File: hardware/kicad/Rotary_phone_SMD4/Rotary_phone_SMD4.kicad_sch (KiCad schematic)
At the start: 64 parts, among them J1 Barrel_Jack_PTH_Slot, J3 PINHD_1x2_Male, J4 PINHD_1x2_Male, J5 PINHD_2x4_Male, J7 PINHD_1x3_Male, J8 RJ12, J9 RJ12, U1 ESP32-C6-DevKitC-1, U2 ES8388, U3 AG1171, U4 AG1171

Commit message: Add SMD4 board support, WiFi setup UX (SSID scan, reset buttons, DHCP hostname)
SMD4 bring-up:
- New board_pins_smd4.h pin map (verified against schematic), Kconfig
  choice, and CMake/preprocessor fixes so es8388/wm8731 build correctly
  for the new board type alongside SMD2/THT.
- Bringup script comment fixes (test_audio.py) for boards past the
  SMD2-only ADC mux bodge.

WiFi/setup UX:
- Live SSID scan (wifi_scan()) with a dropdown picker (+ manual-entry
  fallback) on both the captive setup page and Settings -> General,
  replacing free-text SSID entry.
- Setup AP renamed RotaryPhone-XXXX -> AnalogRedial-XXXX.
- DHCP hostname now set from the board name (was the generic
  "espressif" default) so a router's client list shows something
  identifiable.
- Post-setup confirmation page gives the actual .local address to try
  and recommends the router's client list as a same-weight fallback,
  not a last resort.
- New Settings -> Hardware "Reset" card: re-provision WiFi only (keeps
  all other settings) and a full factory reset (erases all NVS,
  leaves recordings/uploads untouched).

Also: dual idle-power presets, Storage/Diagnostics load-time fixes,
Dial Codes tab redesign, dark-mode link contrast fix, simplified
favicon -- carried over from the same working session.

Co-Authored-By: Claude Sonnet 5 <noreply@anthropic.com>
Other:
- note added: "Fixes needed for SMD4: capacitor silkscreen needs to show capacitance value larger holes for esp32 silkscreen note to add jumpbers for 2nd AG1171"
- note removed: "Fixes: 470 uF capacitors are 8mm/3.5 pitch add reset jumper Fix cross-wired usb D+/D- Connect redundant usb-c wires so cables work in both directions In/out audio lines were swapped! Change Line0/1 in/out to mic for better readability Move Ch2 mic from Lin2 to Rin1 to fix error Todo: cleaner routing for USB D+/D- ? Test use of single P6KE82"
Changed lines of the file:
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@@
 		)
 	)
-	(text "Fixes:\n470 uF capacitors are 8mm/3.5 pitch\nadd reset jumper\nFix cross-wired usb D+/D-\nConnect redundant usb-c wires so cables work in both directions\nIn/out audio lines were swapped!\nChange Line0/1 in/out to mic for better readability\nMove Ch2 mic from Lin2 to Rin1 to fix error\n\nTodo: \ncleaner routing for USB D+/D- ?\nTest use of single P6KE82"
+	(text "Fixes needed for SMD4:\ncapacitor silkscreen needs to show capacitance value\nlarger holes for esp32\nsilkscreen note to add jumpbers for 2nd AG1171\n"
 		(exclude_from_sim no)
 		(at 243.84 41.402 0)

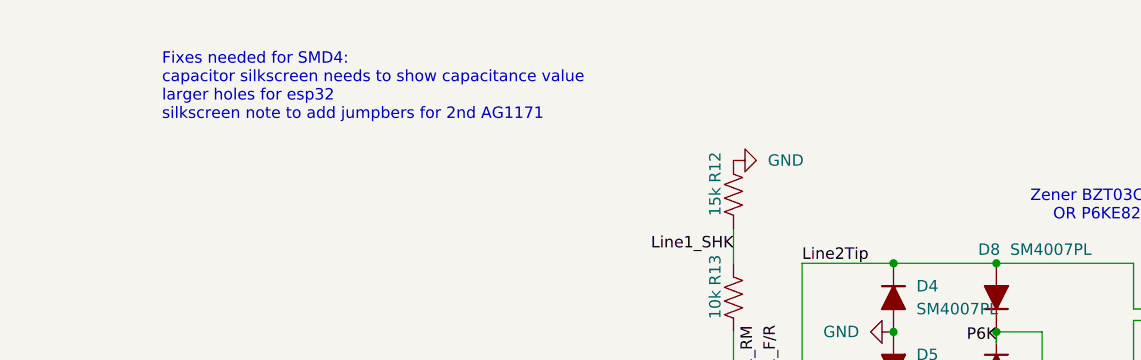
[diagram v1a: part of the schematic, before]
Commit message: Add live memory-map card; fix board type display; simplify hw-config card
- New Settings -> Hardware "Memory map" card: RAM used/free, and every
  flash partition actually in the live partition table (via
  esp_partition_find(), not a copy of partitions.csv baked into the
  UI) with real usage where available (storage/bundled file sizes, NVS
  entry stats) plus a plain answer to "would an 8MB flash chip fit
  this layout" using today's real numbers.
- Fixed two real bugs found while building it: esp_partition_next()
  releases its iterator internally once it reaches the end of the
  list, so an extra esp_partition_iterator_release() call after the
  loop (and, worse, reusing the same iterator across two separate
  loops) double-freed it -- a real, reproducible TLSF heap-corruption
  crash on every load of this card, not a hypothetical. Also fixed two
  fmt_bytes() calls sharing one output buffer as sibling arguments to
  the same snprintf(), which under C's unspecified evaluation order
  could show the wrong figure for RAM total.
- board_hardware_str() always reported "(SMD2)" regardless of which
  PCB the firmware was actually built for -- board_current_type()
  deliberately collapses SMD2/SMD4 into one BOARD_TYPE_SMD (they share
  the line2/microSD GPIO tradeoff), so it was never the right thing to
  read this from. New board_pcb_variant_name() reports the precise
  compile-time PCB name instead, kept separate on purpose.
- Line 2/microSD config card: moved its long explanation from the top
  to the bottom (matching every other settings card's layout) and
  trimmed it to plain language -- no GPIO pin numbers, just "jumpers +
  2nd AG1171" vs "no jumpers, microSD works". Same simplification on
  the first-boot banner's copy of this field.

Co-Authored-By: Claude Sonnet 5 <noreply@anthropic.com>
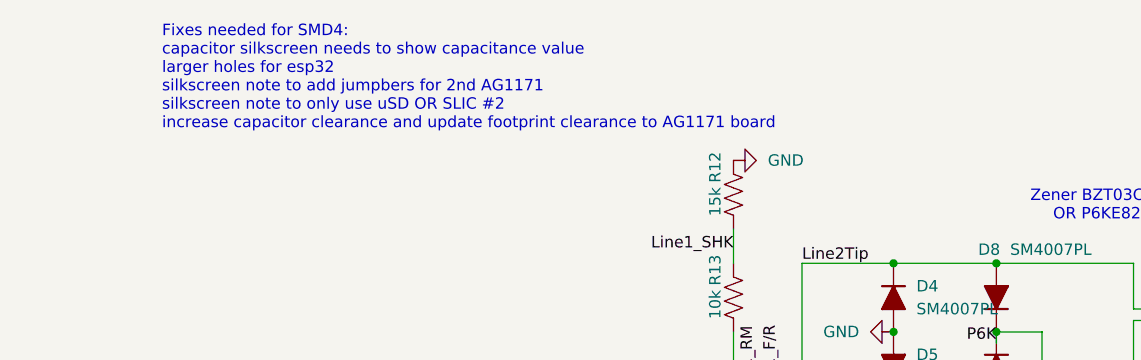
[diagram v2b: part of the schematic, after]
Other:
- note added: "Fixes needed for SMD4: capacitor silkscreen needs to show capacitance value larger holes for esp32 silkscreen note to add jumpbers for 2nd AG1171 silkscreen note to only use uSD OR SLIC #2 increase capacitor clearance and update footprint clearance to AG1171 board"
- note removed: "Fixes needed for SMD4: capacitor silkscreen needs to show capacitance value larger holes for esp32 silkscreen note to add jumpbers for 2nd AG1171"
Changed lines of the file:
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@@
 		)
 	)
-	(text "Fixes needed for SMD4:\ncapacitor silkscreen needs to show capacitance value\nlarger holes for esp32\nsilkscreen note to add jumpbers for 2nd AG1171\n"
+	(text "Fixes needed for SMD4:\ncapacitor silkscreen needs to show capacitance value\nlarger holes for esp32\nsilkscreen note to add jumpbers for 2nd AG1171\nsilkscreen note to only use uSD OR SLIC #2\nincrease capacitor clearance and update footprint clearance to AG1171 board\n\n"
 		(exclude_from_sim no)
 		(at 243.84 41.402 0)

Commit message: kicad: consolidate custom footprints/3D/symbols into libraries/
Move all per-project Scott.pretty, JLCImport.pretty, .3dshapes, and
.kicad_sym files into a single shared kicad/libraries/ directory.
Rename "Scott" library to "Custom" throughout. Update fp-lib-table,
sym-lib-table, .kicad_pcb, and .kicad_sch files in all 6 board
projects to resolve Custom: and JLCImport: via ${KIPRJMOD}/../libraries/.

Also fixes broken 3D model paths (hardcoded /Users/... and
_restore_backup_ references in SMD3/SMD4/AR5 PCBs).

Generated with [Devin](https://devin.ai)

Co-Authored-By: Devin <158243242+devin-ai-integration[bot]@users.noreply.github.com>
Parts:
- J8, J9: footprint Scott:RJ12_Amphenol_87180_Horizontal -> Custom:RJ12_Amphenol_87180_Horizontal
- U3, U4: footprint Scott:AG1171_SIL -> Custom:AG1171_SIL; symbol Scott_Symbol_Library:AG1171_SIL -> Custom_Symbol_Library:AG1171_SIL
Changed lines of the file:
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@@
 			)
 		)
-		(property "Footprint" "Scott:RJ12_Amphenol_87180_Horizontal"
+		(property "Footprint" "Custom:RJ12_Amphenol_87180_Horizontal"
 			(at 364.49 67.945 90)
 			(hide yes)
@@
 			)
 		)
-		(property "Footprint" "Scott:RJ12_Amphenol_87180_Horizontal"
+		(property "Footprint" "Custom:RJ12_Amphenol_87180_Horizontal"
 			(at 367.03 140.335 90)
 			(hide yes)
@@
 	)
 	(symbol
-		(lib_id "Scott_Symbol_Library:AG1171_SIL")
+		(lib_id "Custom_Symbol_Library:AG1171_SIL")
 		(at 308.61 160.02 180)
 		(unit 1)
@@
 			)
 		)
-		(property "Footprint" "Scott:AG1171_SIL"
+		(property "Footprint" "Custom:AG1171_SIL"
 			(at 308.61 160.02 0)
 			(hide yes)
@@
 	)
 	(symbol
-		(lib_id "Scott_Symbol_Library:AG1171_SIL")
+		(lib_id "Custom_Symbol_Library:AG1171_SIL")
 		(at 307.34 87.63 180)
 		(unit 1)
@@
 			)
 		)
-		(property "Footprint" "Scott:AG1171_SIL"
+		(property "Footprint" "Custom:AG1171_SIL"
 			(at 307.34 87.63 0)
 			(hide yes)

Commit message: Consolidate custom KiCad library; point all boards at it
Every custom symbol and footprint this project used to keep in
hardware/kicad/libraries/ (AG1170/AG1171 SIL, the Amphenol/RJ12
connectors, both ESP32-C6 DevKit footprints, WM8731) is now in one
personal library shared across all KiCad projects on this machine:
~/Documents/KiCad/Custom/ (Custom.kicad_sym + Custom.pretty), registered
in KiCad's global symbol/footprint tables under the nickname 'Custom'.
That library also folds in the Schaffner choke, Phoenix terminal, TE
relay and test-point footprints from the old Scott_Library.pretty, and
the BM64 module symbol/footprint from the separate BM64 library.

SMD2, SMD4 and SMD5 ('Analog Redial 5') all used the AG1171_SIL symbol
under a stale 'Custom_Symbol_Library' nickname that was never actually
registered anywhere live (only resolvable from each schematic's own
embedded symbol cache) -- renamed to 'Custom:AG1171_SIL' in all three
schematics to match the new global library's nickname, which footprint
references already used. Verified with kicad-cli: netlist export clean
on all three, PCB export unaffected.

SMD2's project-local sym-lib-table/fp-lib-table had their own
'Custom_Symbol_Library'/'Custom' entries pointing at the
now-superseded repo copy -- removed, so it falls through to the
global table like SMD4/SMD5 already did. SMD4 and SMD5 never had
project-local entries for these, so no table changes were needed
there beyond the rename.

The old repo copy moves to
archive/hardware/kicad-libraries-pre-consolidation/ rather than being
deleted, per the project's archive convention -- its README explains
what superseded it and what a fresh clone still gets (schematics/PCBs
embed their own symbol/footprint copies, so they still open, view,
and export Gerbers/BOM fine; only live library editing needs the
global Custom library now).

Not touched: the untracked 'Analog Redial v6' board (newer WIP, not
yet added to git) got the same nickname rename and had its own stale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
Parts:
- U3, U4: symbol Custom_Symbol_Library:AG1171_SIL -> Custom:AG1171_SIL
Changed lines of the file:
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@@
 	)
 	(symbol
-		(lib_id "Custom_Symbol_Library:AG1171_SIL")
+		(lib_id "Custom:AG1171_SIL")
 		(at 308.61 160.02 180)
 		(unit 1)
@@
 	)
 	(symbol
-		(lib_id "Custom_Symbol_Library:AG1171_SIL")
+		(lib_id "Custom:AG1171_SIL")
 		(at 307.34 87.63 180)
 		(unit 1)
